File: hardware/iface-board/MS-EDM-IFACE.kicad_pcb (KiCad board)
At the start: 2 copper layers, 110 x 80 mm, 35 parts, among them J1 TO_PIBOT, J2 TO_PIBOT_BC, J3 CAN, J4 LOADCELL, Q1 MMBT3904, U1 MCP2518FD, U2 TJA1051T-3, U3 HX711, Y1 40MHz

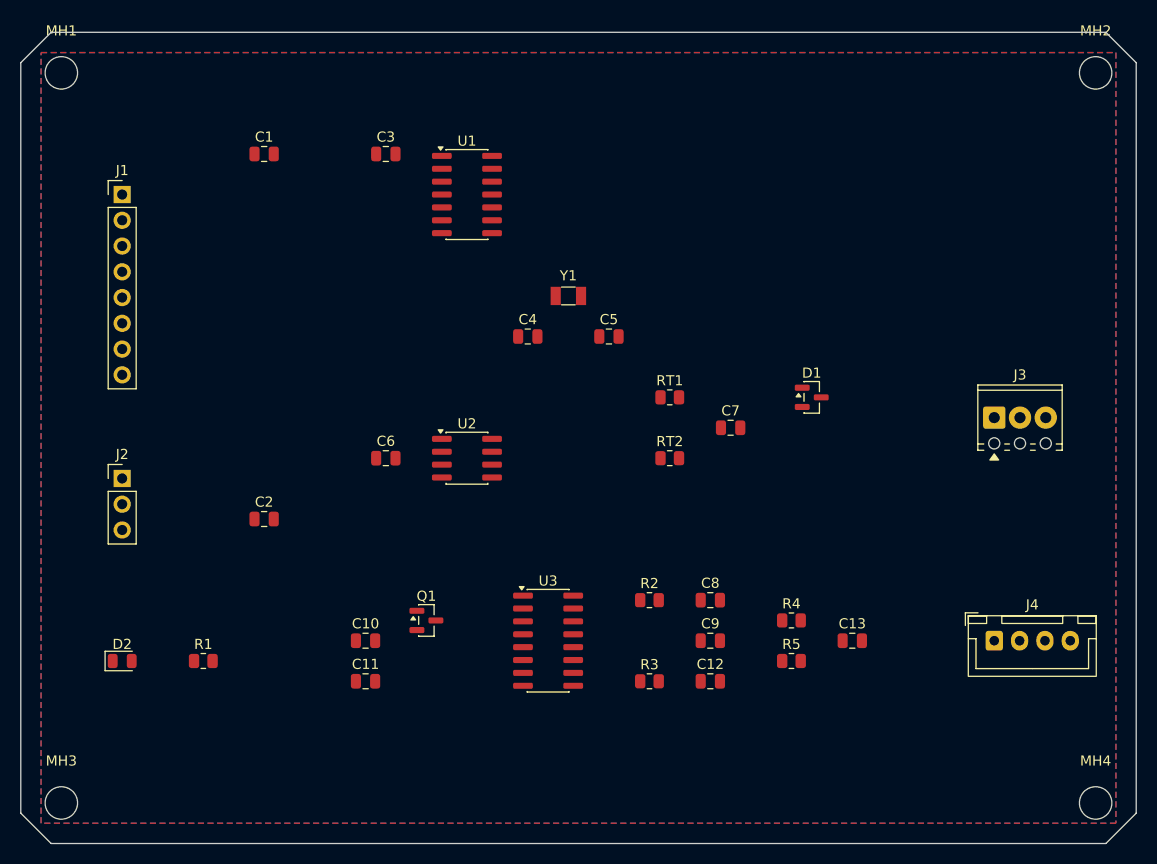
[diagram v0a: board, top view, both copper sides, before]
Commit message: hw(iface-board): PCB routing updates, Specctra DSN/SES and route script
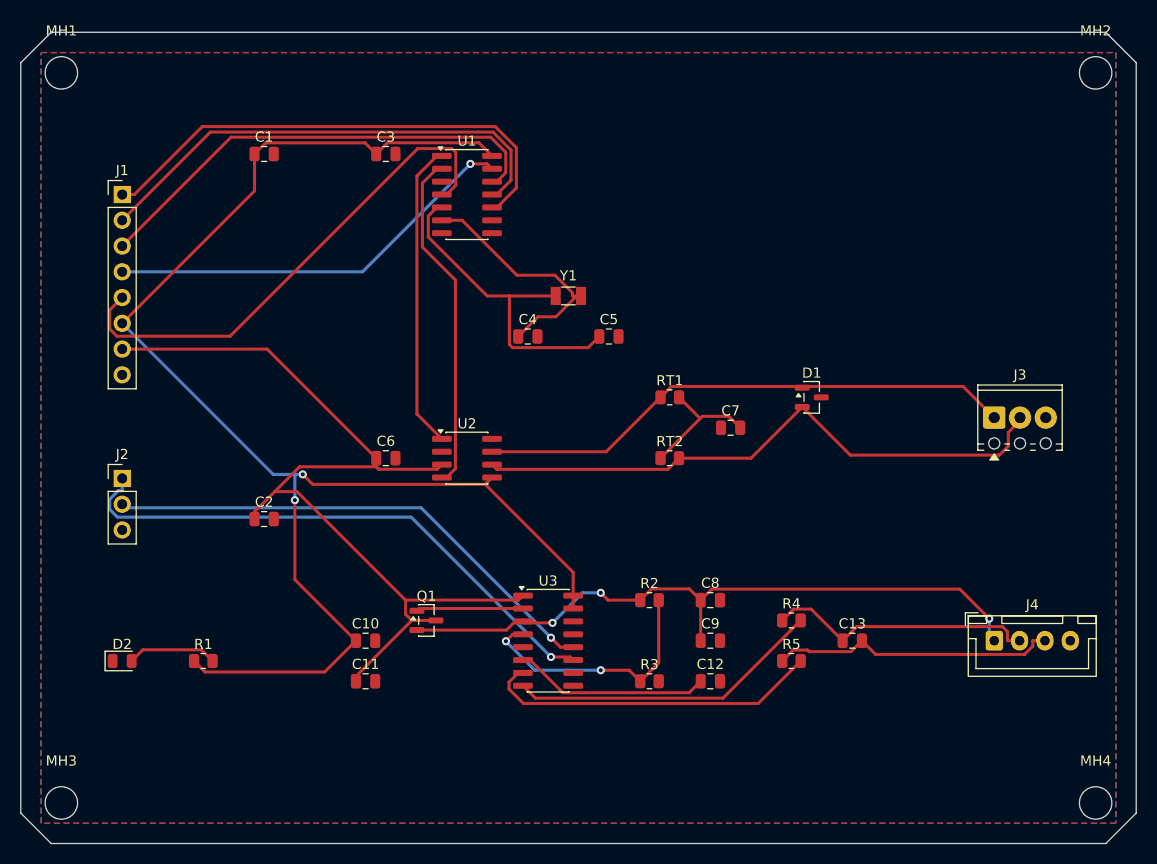
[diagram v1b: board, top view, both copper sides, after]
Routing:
- net +3V3: track 0.00 -> 143.2 mm, vias 0 -> 2
- net +5V: track 0.00 -> 93.7 mm
- net AVDD: track 0.00 -> 67.3 mm, vias 0 -> 3
- net CANL: track 0.00 -> 59.3 mm
- net HX_SCK: track 0.00 -> 55.6 mm, vias 0 -> 1
- net CANH: track 0.00 -> 53.7 mm
- net MCP_INT: track 0.00 -> 50.8 mm
- net HX_DOUT: track 0.00 -> 50.3 mm, vias 0 -> 1
- net SPI_SCK: track 0.00 -> 49.7 mm
- net SPI_MOSI: track 0.00 -> 48.1 mm
- net SPI_MISO: track 0.00 -> 46.6 mm
- net MCP_CS: track 0.00 -> 41.1 mm, vias 0 -> 1
- net MCP_RXCAN: track 0.00 -> 33.7 mm
- net INA_N: track 0.00 -> 33.5 mm
- net OSC2: track 0.00 -> 33.0 mm
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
